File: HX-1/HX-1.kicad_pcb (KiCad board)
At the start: 2 copper layers, 45 x 90 mm, 90 parts, among them J1 USB_C_Receptacle_USB2.0_16P, J10 Conn_01x24, J12 USART, J2 Conn_01x02_Socket, J3 I2C, J4 SPI, J8 UART, J9 Conn_01x24, SW1 BOOT0, U1 STM32H723ZGT6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

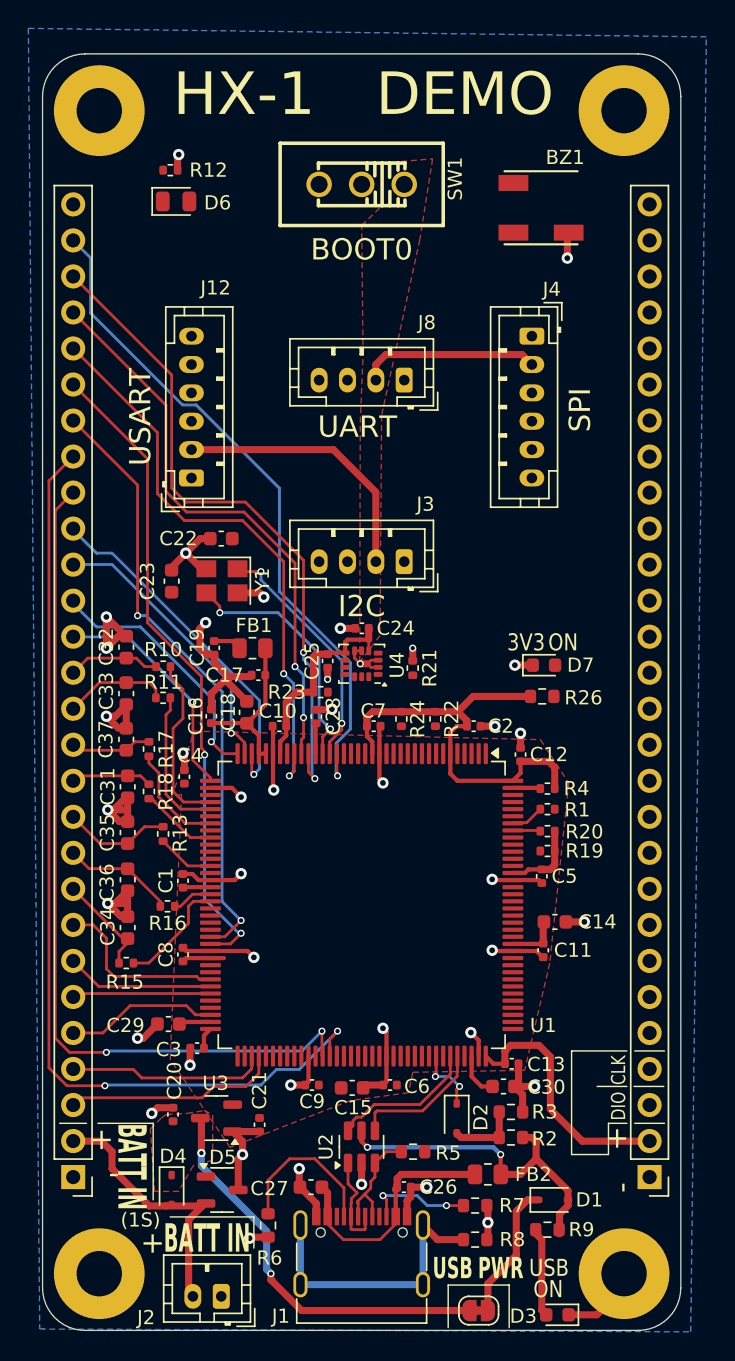
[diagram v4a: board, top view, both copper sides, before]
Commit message: complete route of left side of board, flip cts and rts pins on jst connector
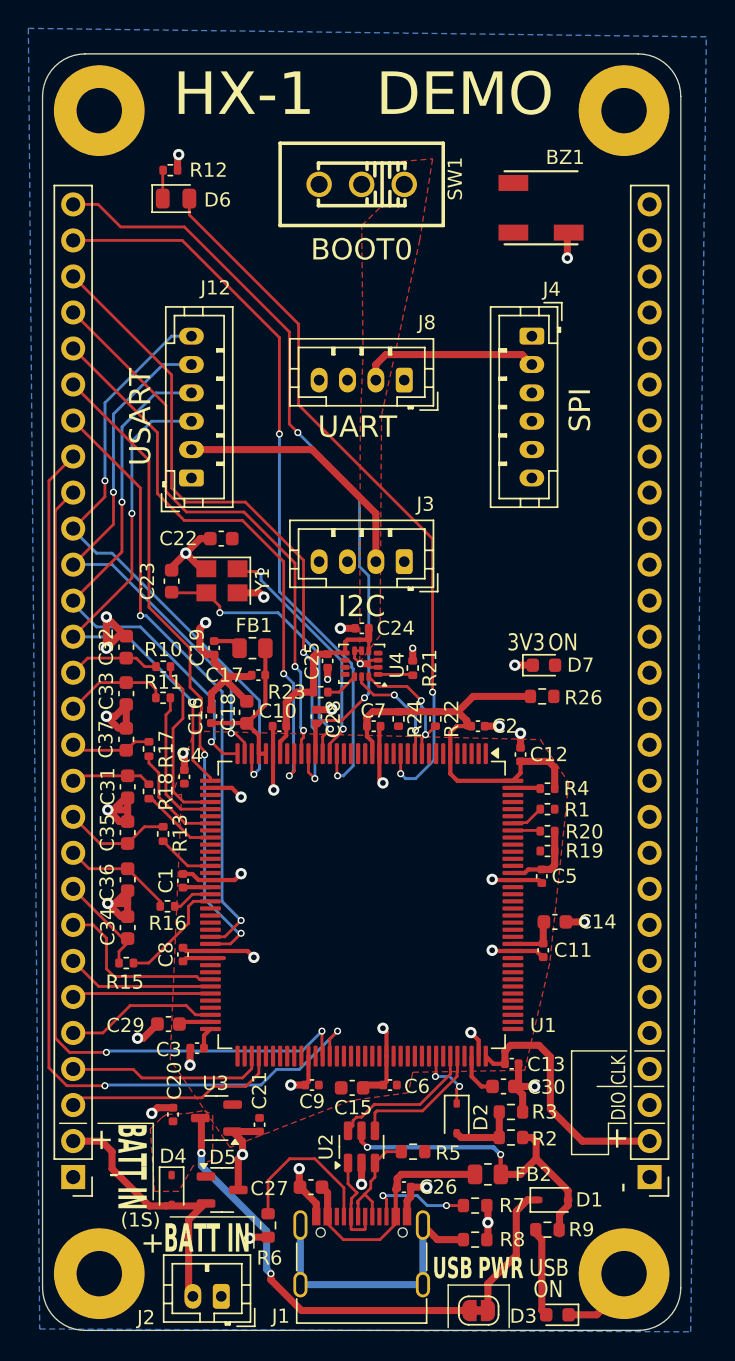
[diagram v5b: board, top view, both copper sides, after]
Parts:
- moved C2 0.30 mm to (157.7, 122.2)
- moved R24 0.20 mm to (152.1, 121.7)
- moved D6 0.20 mm to (136.4, 85.0)
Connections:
- J12 pad 5: /MCU/USART2_CTS -> /MCU/USART2_RTS
- J12 pad 6: /MCU/USART2_RTS -> /MCU/USART2_CTS
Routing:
- net /MCU/NRST: track 2.16 -> 53.5 mm, vias 0 -> 2
- net TIM23_LED: track 0.00 -> 51.0 mm, vias 0 -> 2
- net /MCU/USART2_RX: track 16.4 -> 36.7 mm, vias 1 -> 2
- net /MCU/USART2_TX: track 18.2 -> 37.7 mm, vias 1 -> 2
- net /MCU/USART2_RTS: track 20.1 -> 38.9 mm, vias 1 -> 2
- net /MCU/USART2_CTS: track 25.8 -> 43.6 mm, vias 1 -> 2
- net I2C2_SDA: track 0.00 -> 9.31 mm, vias 0 -> 2
- net I2C2_SCL: track 0.00 -> 7.87 mm, vias 0 -> 2
- net /MCU/GPIO_8: track 48.4 -> 52.7 mm, vias 1 -> 2
- net RCC_OSC_OUT: track 17.6 -> 20.1 mm
- net /Communication and Debug/LSM_SDO: track 0.00 -> 2.46 mm
- net /Communication and Debug/LSM_CS: track 0.00 -> 2.33 mm
- net /Communication and Debug/G_LED_anode: track 0.00 -> 2.21 mm
- net +3.3V: track 113.2 -> 112.4 mm

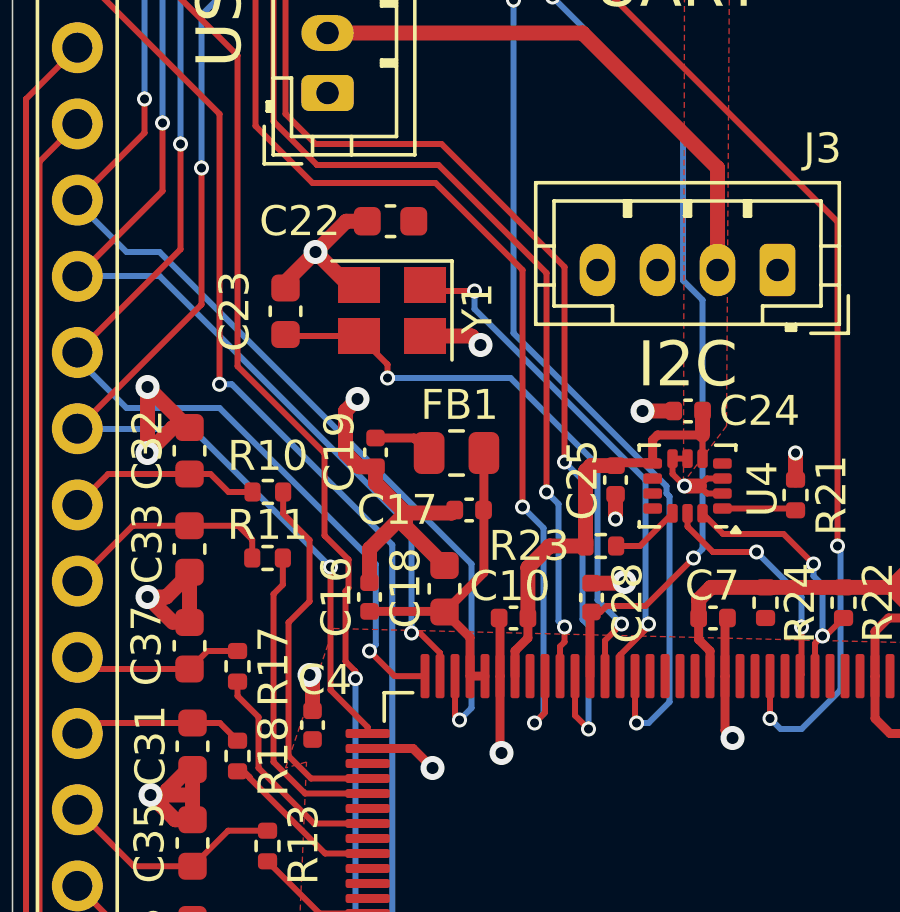
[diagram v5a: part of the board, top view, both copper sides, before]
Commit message: rearrange some analog voltage components, connect missing 3v3 traces
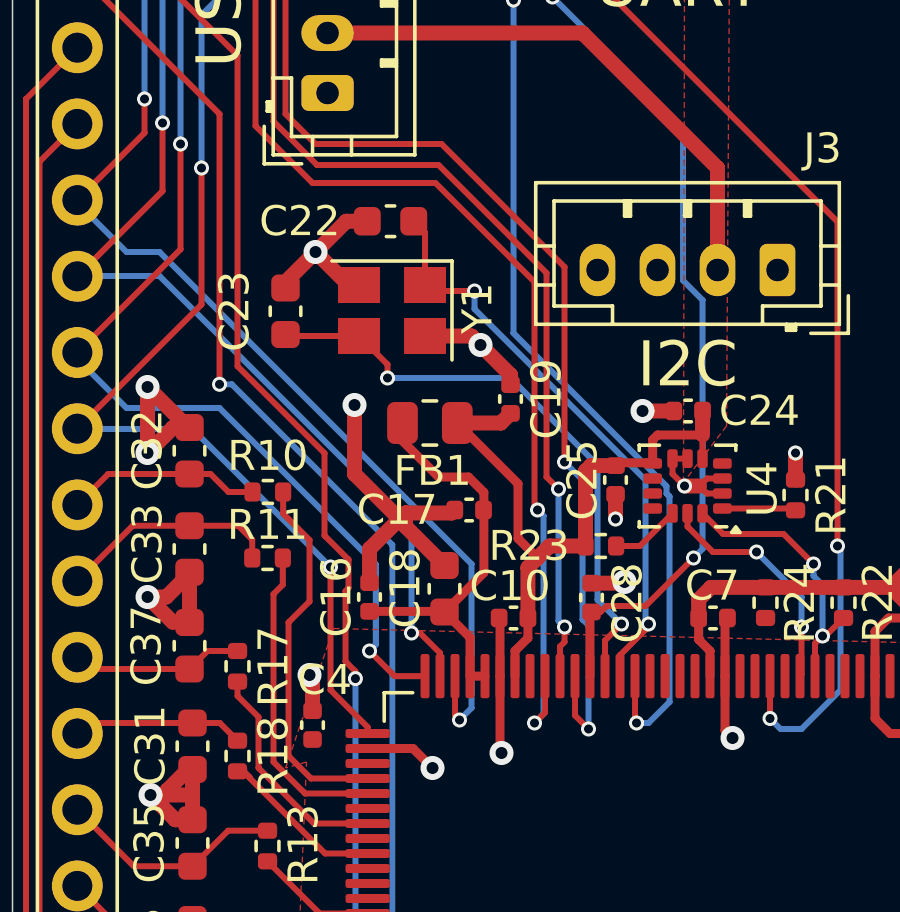
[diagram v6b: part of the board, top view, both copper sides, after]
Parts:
- moved C19 4.84 mm to (143.6, 114.9), turned to 90 degrees
- moved FB1 1.34 mm to (140.9, 115.7), turned to 0 degrees
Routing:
- net +3.3V: track 112.4 -> 118.0 mm
- net +3.3VA: track 11.3 -> 14.1 mm
- net RCC_OSC_IN: track 17.4 -> 19.6 mm
- net GND: track 131.2 -> 132.2 mm

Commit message: trace some of the right side pins
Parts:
- moved R4 0.67 mm to (162.9, 126.0)
- moved R1 0.58 mm to (162.8, 127.5)
- moved R20 0.44 mm to (163.0, 129.4), turned to 180 degrees
- moved R19 0.40 mm to (163.0, 130.9), turned to 180 degrees
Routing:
- net /MCU/GPIO_6: track 0.00 -> 51.5 mm, vias 0 -> 2
- net /MCU/GPIO_7/DAC_EXT: track 0.00 -> 46.5 mm, vias 0 -> 2
- net TIM23_BUZZ: track 0.00 -> 44.1 mm, vias 0 -> 4
- net /MCU/I2C_SCL: track 0.00 -> 43.7 mm, vias 0 -> 4
- net /MCU/I2C_SDA: track 1.74 -> 42.9 mm, vias 0 -> 2
- net /MCU/TIM4_PWM_1: track 0.00 -> 31.3 mm, vias 0 -> 2
- net /MCU/TIM4_PWM_2: track 0.00 -> 29.6 mm, vias 0 -> 2
- net /MCU/DEBUG_SWDIO: track 0.00 -> 15.9 mm, vias 0 -> 1
- net /MCU/TIM2_PWM_2: track 0.00 -> 12.3 mm, vias 0 -> 2
- net /MCU/TIM23_PWM_2: track 0.00 -> 11.9 mm
- net /MCU/TIM23_PWM_1: track 0.00 -> 11.1 mm
- net /MCU/DEBUG_SWCLK: track 0.00 -> 10.8 mm
- net /MCU/FDCAN1_TX: track 0.00 -> 10.4 mm
- net /MCU/TIM2_PWM_1: track 0.00 -> 9.96 mm
- net /MCU/FDCAN1_RX: track 0.00 -> 9.74 mm
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
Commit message: replace right header pin for BOOT with GND, remove PIN control of BOOT for simplicity
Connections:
- J9 pad 28: /MCU/BOOT0 -> GND
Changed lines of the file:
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@@
 			)
 			(remove_unused_layers no)
-			(net 40 "/MCU/BOOT0")
+			(net 3 "GND")
 			(pinfunction "Pin_28")
 			(pintype "passive")
